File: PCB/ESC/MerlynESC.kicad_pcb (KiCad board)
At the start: 6 copper layers, 30.5 x 31.9 mm, 155 parts, among them M1 BLDC Motor, M2 BLDC Motor, M3 BLDC Motor, M4 BLDC Motor, Q1 JMSL0302AU, Q10 JMSL0302AU, Q11 JMSL0302AU, Q12 JMSL0302AU, Q13 JMSL0302AU, Q14 JMSL0302AU, Q15 JMSL0302AU, Q16 JMSL0302AU, Q17 JMSL0302AU, Q18 JMSL0302AU, Q19 JMSL0302AU, Q2 JMSL0302AU, Q20 JMSL0302AU, Q21 JMSL0302AU, Q22 JMSL0302AU, Q23 JMSL0302AU, Q24 JMSL0302AU, Q3 JMSL0302AU, Q4 JMSL0302AU, Q5 JMSL0302AU, Q6 JMSL0302AU, Q7 JMSL0302AU, Q8 JMSL0302AU, Q9 JMSL0302AU, U1 HT75C0-1, U10 EG6288, U11 EFM8BB21F16G, U2 HT7533-1, U3 EFM8BB21F16G, U4 EG6288, U5 EG6288, U6 EFM8BB21F16G, U7 INA139NA, U8 EG6288, U9 EFM8BB21F16G

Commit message: checkpoint
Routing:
- net +BATT: track 3.82 -> 29.4 mm, vias 19 -> 57
- net Net-(Q18-G): track 9.98 -> 11.7 mm
- net Net-(Q9-G): track 5.95 -> 7.31 mm
- net Net-(Q7-G): track 7.12 -> 8.04 mm
- net Net-(Q15-G): track 5.96 -> 6.80 mm
- net M3_PHASE2: track 8.40 -> 9.22 mm, vias 7 -> 6
- net M1_PHASE2: track 9.08 -> 9.81 mm, vias 7 -> 6
- net M4_PHASE2: track 7.31 -> 8.00 mm, vias 7 -> 6
- net M2_PHASE2: track 5.99 -> 6.47 mm, vias 7 -> 6
- net GND: vias 56 -> 79

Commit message: checkpoint
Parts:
- added H1: C2CK, easyeda2kicad:TestPoint, F.Cu at (156.4, 102.5)
- added H2: C2D, easyeda2kicad:TestPoint, F.Cu at (155.7, 102.5)
- added H4: C2CK, easyeda2kicad:TestPoint, F.Cu at (156.6, 96.1)
- added H5: C2D, easyeda2kicad:TestPoint, F.Cu at (155.9, 96.0)
- added H6: C2CK, easyeda2kicad:TestPoint, F.Cu at (155.5, 108.4)
- added H7: C2D, easyeda2kicad:TestPoint, F.Cu at (155.5, 107.6)
- added H8: C2CK, easyeda2kicad:TestPoint, F.Cu at (154.2, 101.3)
- added H9: C2D, easyeda2kicad:TestPoint, F.Cu at (155.1, 101.3)
- moved C20 0.47 mm to (156.6, 108.2)
- moved R34 0.40 mm to (154.3, 108.0)
- moved C21 0.25 mm to (157.8, 108.6)
- moved U7 0.25 mm to (155.4, 110.1)
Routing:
- net +12V: track 110.8 -> 115.1 mm
- net +3.3V: track 43.1 -> 46.1 mm
- net M1_C2D: track 0.00 -> 1.96 mm
- net M2_C2D: track 0.00 -> 1.94 mm
- net M4_C2D: track 0.00 -> 1.83 mm
- net M3_C2D: track 0.00 -> 1.70 mm
- net M3_C2CK: track 1.15 -> 2.67 mm
- net Net-(U7-OUT): track 20.3 -> 21.7 mm
- net M4_C2CK: track 1.09 -> 2.23 mm, vias 1 -> 0
- net M4_DSHOT: track 18.0 -> 19.1 mm
- net M2_DSHOT: track 15.4 -> 16.5 mm
- net M3_DSHOT: track 23.5 -> 24.6 mm
- net M1_C2CK: track 1.15 -> 2.02 mm
- net M2_C2CK: track 1.15 -> 1.99 mm, vias 1 -> 0
- net GND: track 27.6 -> 28.0 mm, vias 79 -> 123
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
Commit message: checkpoint
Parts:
- C1: footprint Capacitor_SMD:C_0805_2012Metric -> easyeda2kicad:C_0805_2012Metric
- C2, C9: footprint Capacitor_SMD:C_0603_1608Metric -> easyeda2kicad:C_0603_1608Metric
- C3, C4, C5, C6, C7, C8: footprint Capacitor_SMD:C_1206_3216Metric -> easyeda2kicad:C_1206_3216Metric
- D1, D10, D11, D12, D2, D3, D4, D5, D6, D7, D8, D9: footprint Diode_SMD:D_SOD-923 -> easyeda2kicad:D_SOD-923
- moved H7 0.14 mm to (155.6, 107.6)
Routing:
- net +BATT: track 29.4 -> 30.2 mm
- net M3_PHASE1: track 10.3 -> 9.65 mm
- net CSense: track 6.49 -> 7.06 mm
- net M3_PHASE2: track 9.22 -> 8.71 mm
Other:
- board text added: "+"
- board text added: "-"
- board text added: "1"
- board text added: "2"
- board text added: "3"
- board text added: "4"
- board text added: ":3"
- board text added: "MerlynESC"

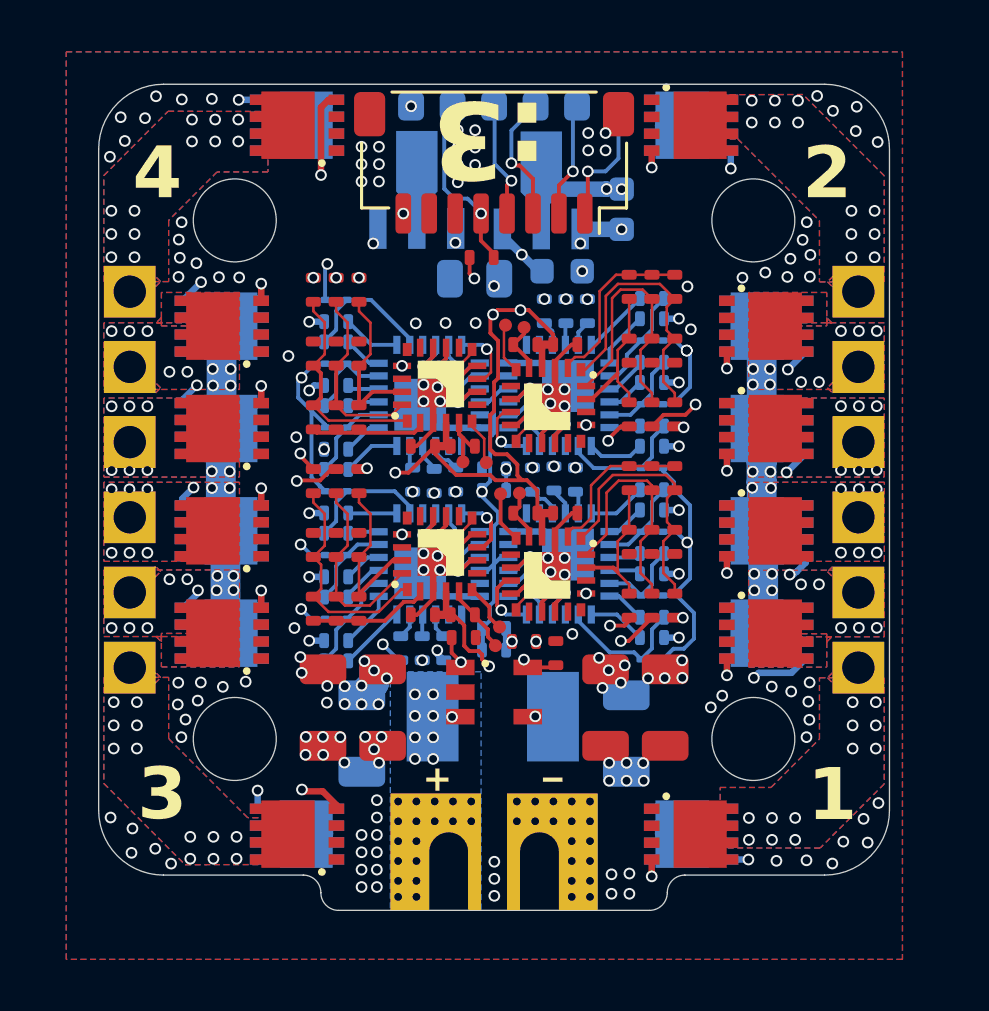
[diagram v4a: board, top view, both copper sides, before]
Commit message: ESC Rev 2. Connected gate driver VS pin to motor phase
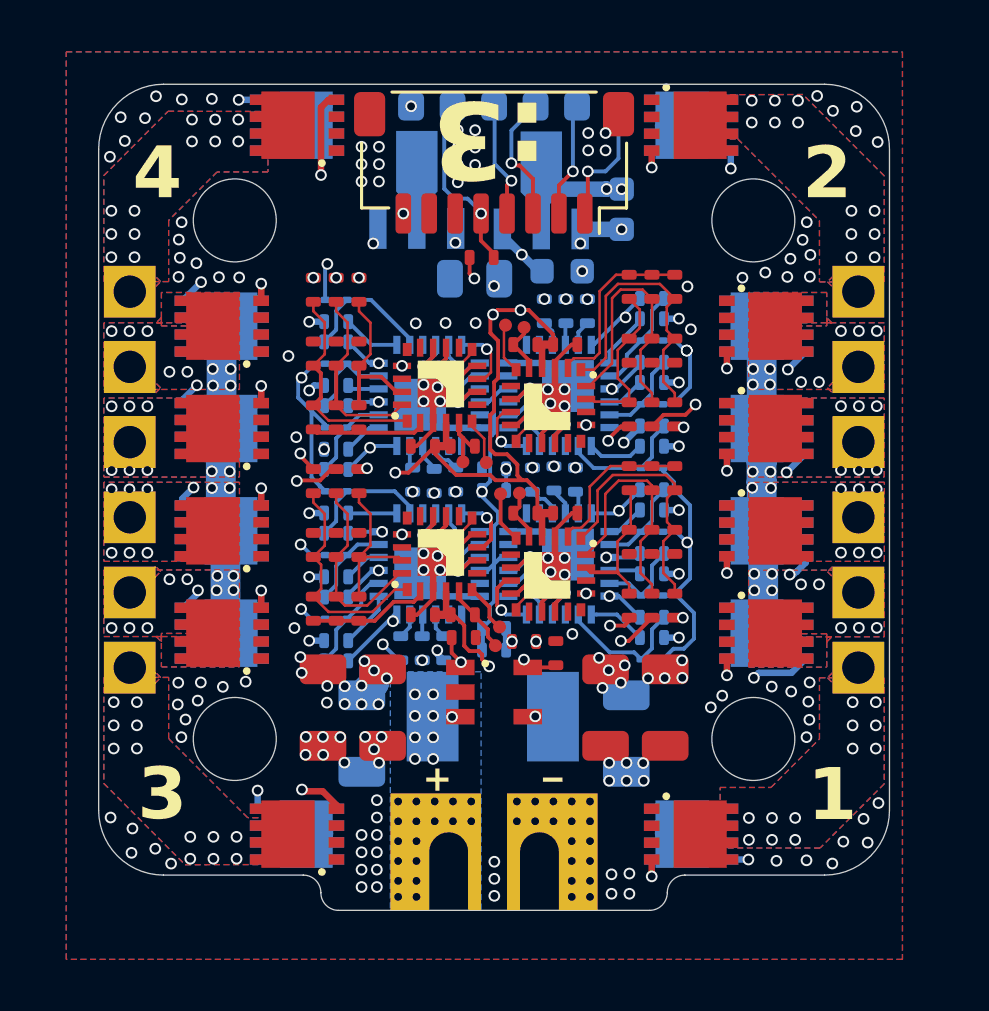
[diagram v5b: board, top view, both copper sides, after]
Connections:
- C11 pad 1: Net-(U4-VS1) -> M1_PHASE1
- C12 pad 1: Net-(U4-VS2) -> M1_PHASE2
- C13 pad 1: Net-(U4-VS3) -> M1_PHASE3
- C17 pad 1: Net-(U5-VS1) -> M2_PHASE1
- C18 pad 1: Net-(U5-VS2) -> M2_PHASE2
- C19 pad 1: Net-(U5-VS3) -> M2_PHASE3
- C24 pad 1: Net-(U8-VS1) -> M3_PHASE1
- C25 pad 1: Net-(U8-VS2) -> M3_PHASE2
- C26 pad 1: Net-(U8-VS3) -> M3_PHASE3
- C29 pad 1: Net-(U10-VS1) -> M4_PHASE1
- C30 pad 1: Net-(U10-VS2) -> M4_PHASE2
- C31 pad 1: Net-(U10-VS3) -> M4_PHASE3
- U10 pad 12: Net-(U10-VS3) -> M4_PHASE3
- U10 pad 15: Net-(U10-VS2) -> M4_PHASE2
- U10 pad 18: Net-(U10-VS1) -> M4_PHASE1
- U4 pad 12: Net-(U4-VS3) -> M1_PHASE3
- U4 pad 15: Net-(U4-VS2) -> M1_PHASE2
- U4 pad 18: Net-(U4-VS1) -> M1_PHASE1
- U5 pad 12: Net-(U5-VS3) -> M2_PHASE3
- U5 pad 15: Net-(U5-VS2) -> M2_PHASE2
- U5 pad 18: Net-(U5-VS1) -> M2_PHASE1
- U8 pad 12: Net-(U8-VS3) -> M3_PHASE3
- U8 pad 15: Net-(U8-VS2) -> M3_PHASE2
- U8 pad 18: Net-(U8-VS1) -> M3_PHASE1
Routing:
- net M3_PHASE3: track 17.4 -> 31.8 mm, vias 13 -> 14
- net M4_PHASE1: track 7.91 -> 20.2 mm, vias 13 -> 14
- net M2_PHASE3: track 16.0 -> 28.0 mm, vias 13 -> 14
- net M4_PHASE3: track 11.1 -> 22.6 mm, vias 7 -> 8
- net M2_PHASE2: track 6.50 -> 17.9 mm, vias 6 -> 7
- net M1_PHASE3: track 11.3 -> 22.7 mm, vias 7 -> 8
- net M4_PHASE2: track 8.05 -> 19.3 mm, vias 6 -> 7
- net M3_PHASE1: track 9.65 -> 20.8 mm, vias 7 -> 8
- net M1_PHASE2: track 9.55 -> 19.7 mm, vias 6 -> 7
- net M3_PHASE2: track 8.71 -> 18.2 mm, vias 6 -> 7
- net M1_PHASE1: track 9.09 -> 13.8 mm, vias 13 -> 14
- net M2_PHASE1: track 6.90 -> 11.6 mm, vias 7 -> 8
- net Net-(U8-VS3): track 2.62 -> 0.00 mm
- net Net-(U5-VS3): track 2.62 -> 0.00 mm
- net Net-(U4-VS3): track 2.25 -> 0.00 mm
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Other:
- board text added: "Rev 2"
